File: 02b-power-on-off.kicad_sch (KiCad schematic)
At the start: 13 parts, among them Q1 DMG2305UX-7, Q2 DMG2305UX-7, Q3 BSS138, SW5 SW_Push

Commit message: Add proper charging detection, fix zener footprint
Connect the BQ25 status pin to the microcontroller for a proper
charging detection (low active).
Correct the footprint for the selected zener diode.
Somehow, the wrong footprint got assigned.
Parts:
- D6: footprint Diode_SMD:Nexperia_CFP3_SOD-123W -> prj-footprints:DIO_TDZVT_ROM
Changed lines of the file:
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@@
 			)
 		)
-		(property "Footprint" "Diode_SMD:Nexperia_CFP3_SOD-123W"
+		(property "Footprint" "prj-footprints:DIO_TDZVT_ROM"
 			(at 209.55 120.65 0)
 			(effects

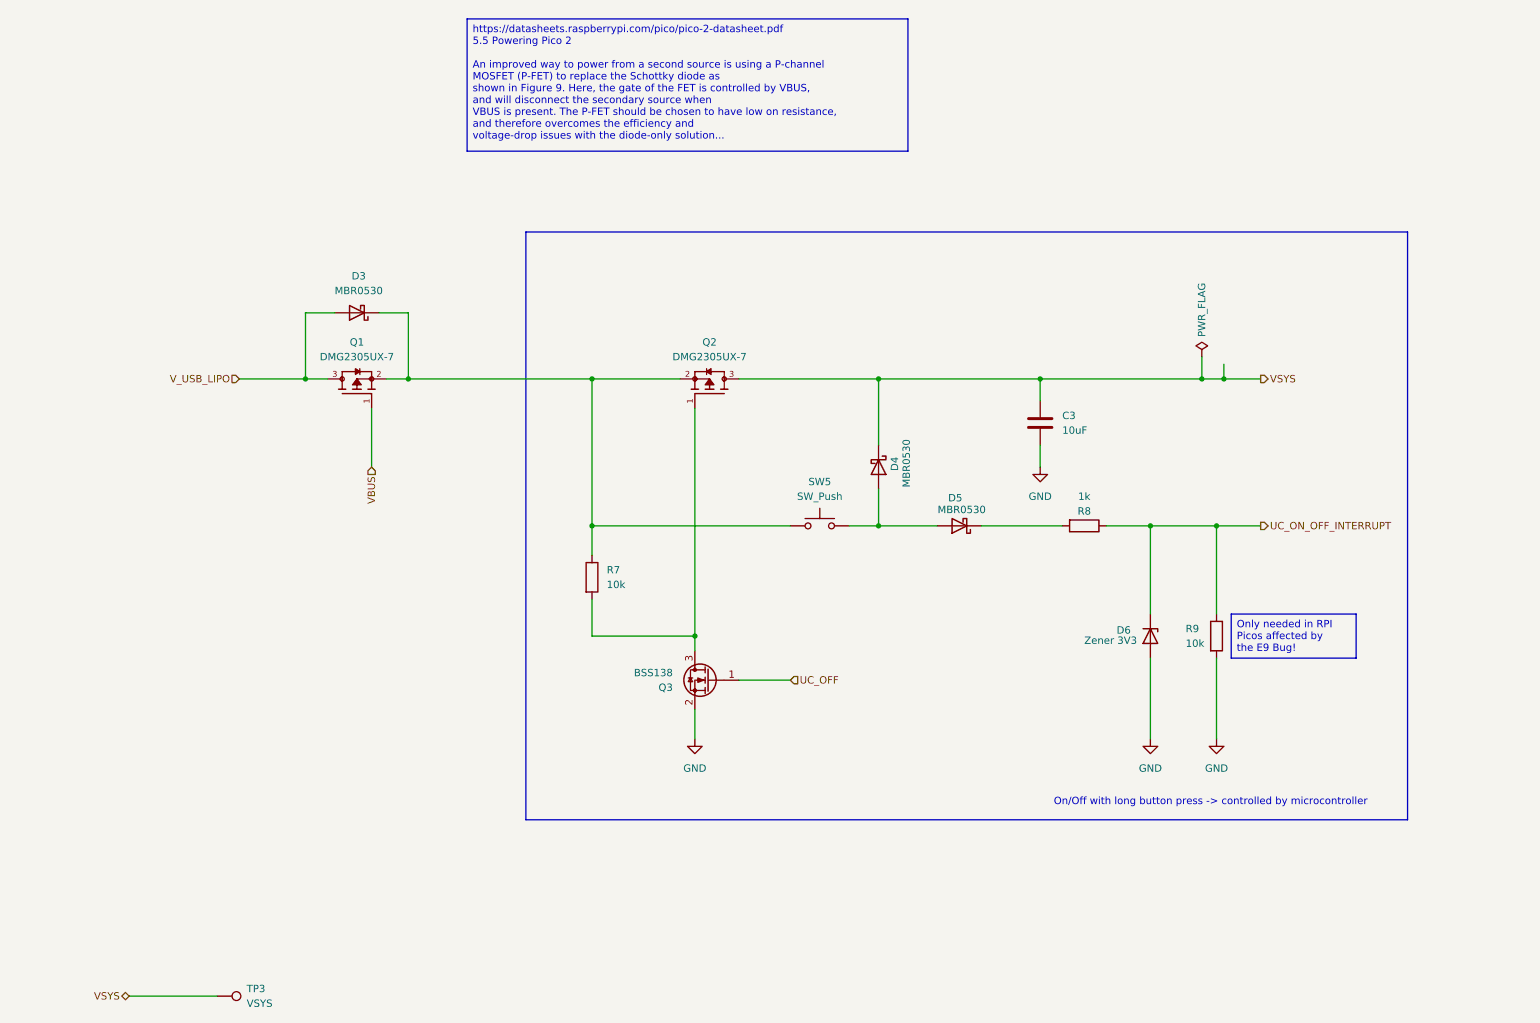
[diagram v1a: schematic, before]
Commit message: Add an voltage bypass mode when USB-C is connected
When USB-C is connected, the device should be charging, but also powered,
without taking care of the on/off button's state.
Otherwise, flashing the device via USB-C would only be
possible as long as the button is pressed which makes the usage
experience a mess and flaky.
This uses p-MOSFETs to do the switch and
a) avoid a battery voltage going to the system when USB-C is connected
b) avoid powering having both, USB-C and Micro-USB active

TODO: This adds the basic idea, routing must be fixed!
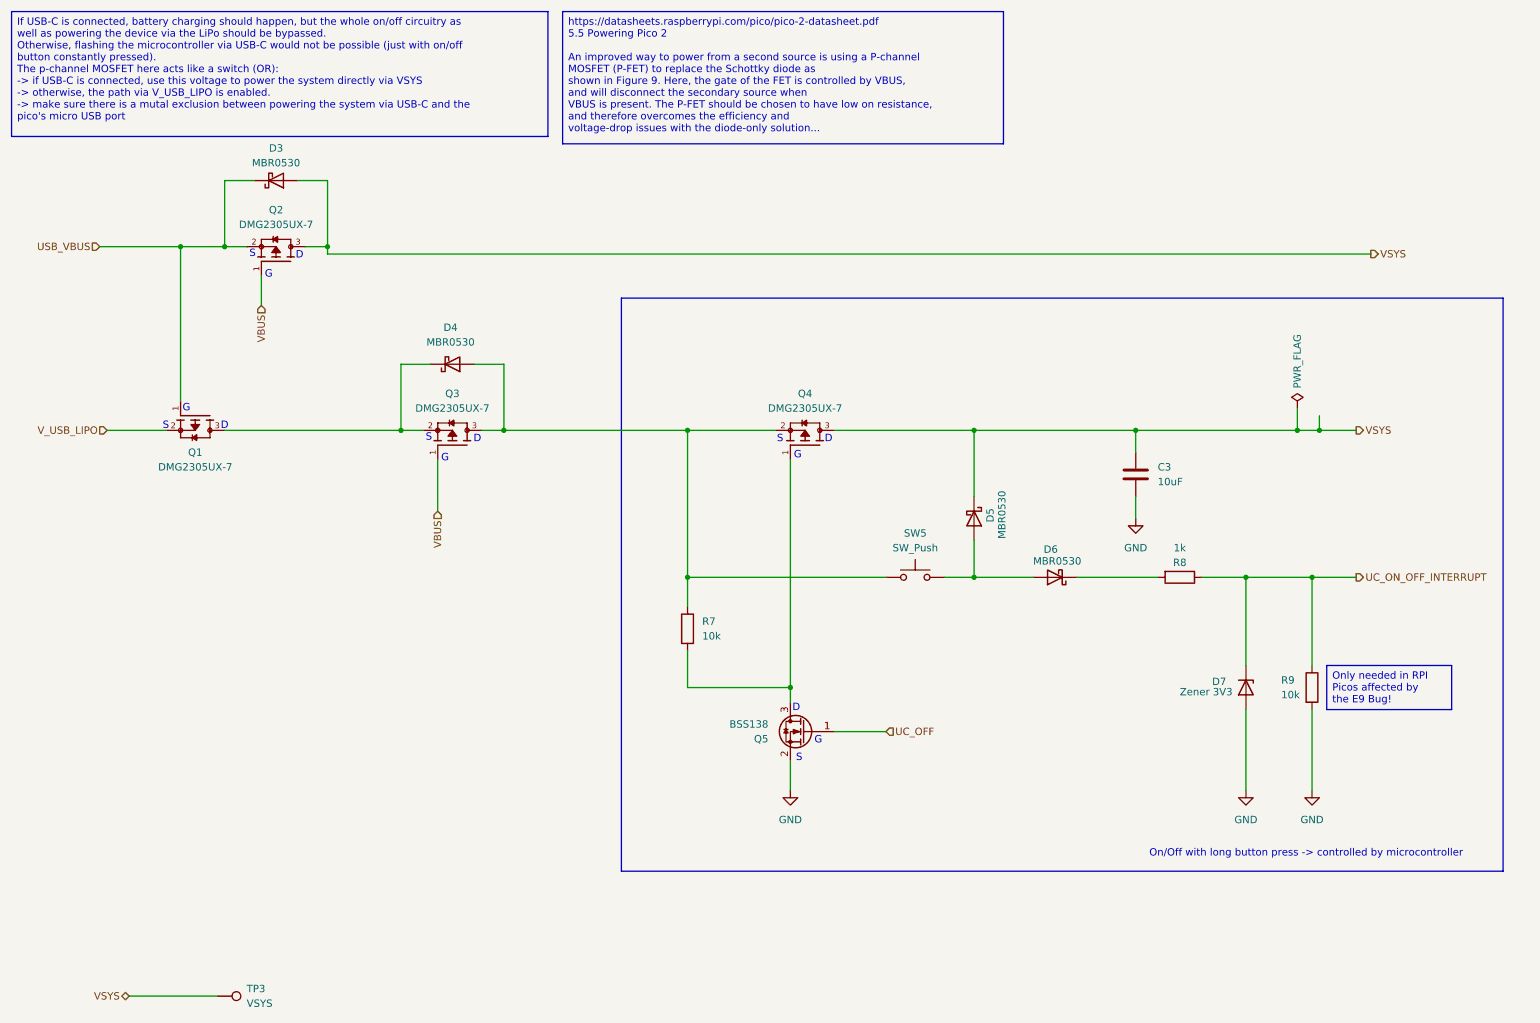
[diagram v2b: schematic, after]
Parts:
- added D3: MBR0530, Diode_SMD:D_SOD-123, symbol Diode:MBR0530
- added Q1, Q2: DMG2305UX-7, Package_TO_SOT_SMD:SOT-23-3, symbol DMG2305UX-7:DMG2305UX-7
- renumbered D3 to D4, D4 to D5, D5 to D6, D6 to D7, Q1 to Q3, Q2 to Q4, Q3 to Q5
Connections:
- net VBUS: now also Q2.1
- net VSYS: now also D3.2 (A), Q2.3
- net V_USB_LIPO: now also Q1.2; no longer D4.2 (A), Q3.3
- net at Q4.2, R7.1, SW5.1: now also D4.2 (A), Q3.3; no longer D4.1 (K), Q3.2
- new net: D4.1 (K), Q1.3, Q3.2
- new net USB_VBUS: D3.1 (K), Q1.1, Q2.2
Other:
- note added: "D"
- note added: "G"
- note added: "S"
- moved on the sheet: C3, D4, D5, D6, D7, Q3, Q4, Q5, R7, R8, R9, SW5

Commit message: Introduce KiCad native Jobsets as an alternative to KiBot
Adds KiCad a jobset together with a new GitHub workflow file
to generate the project outputs without external tooling.

Some general work on the USB-Powerpath routing.
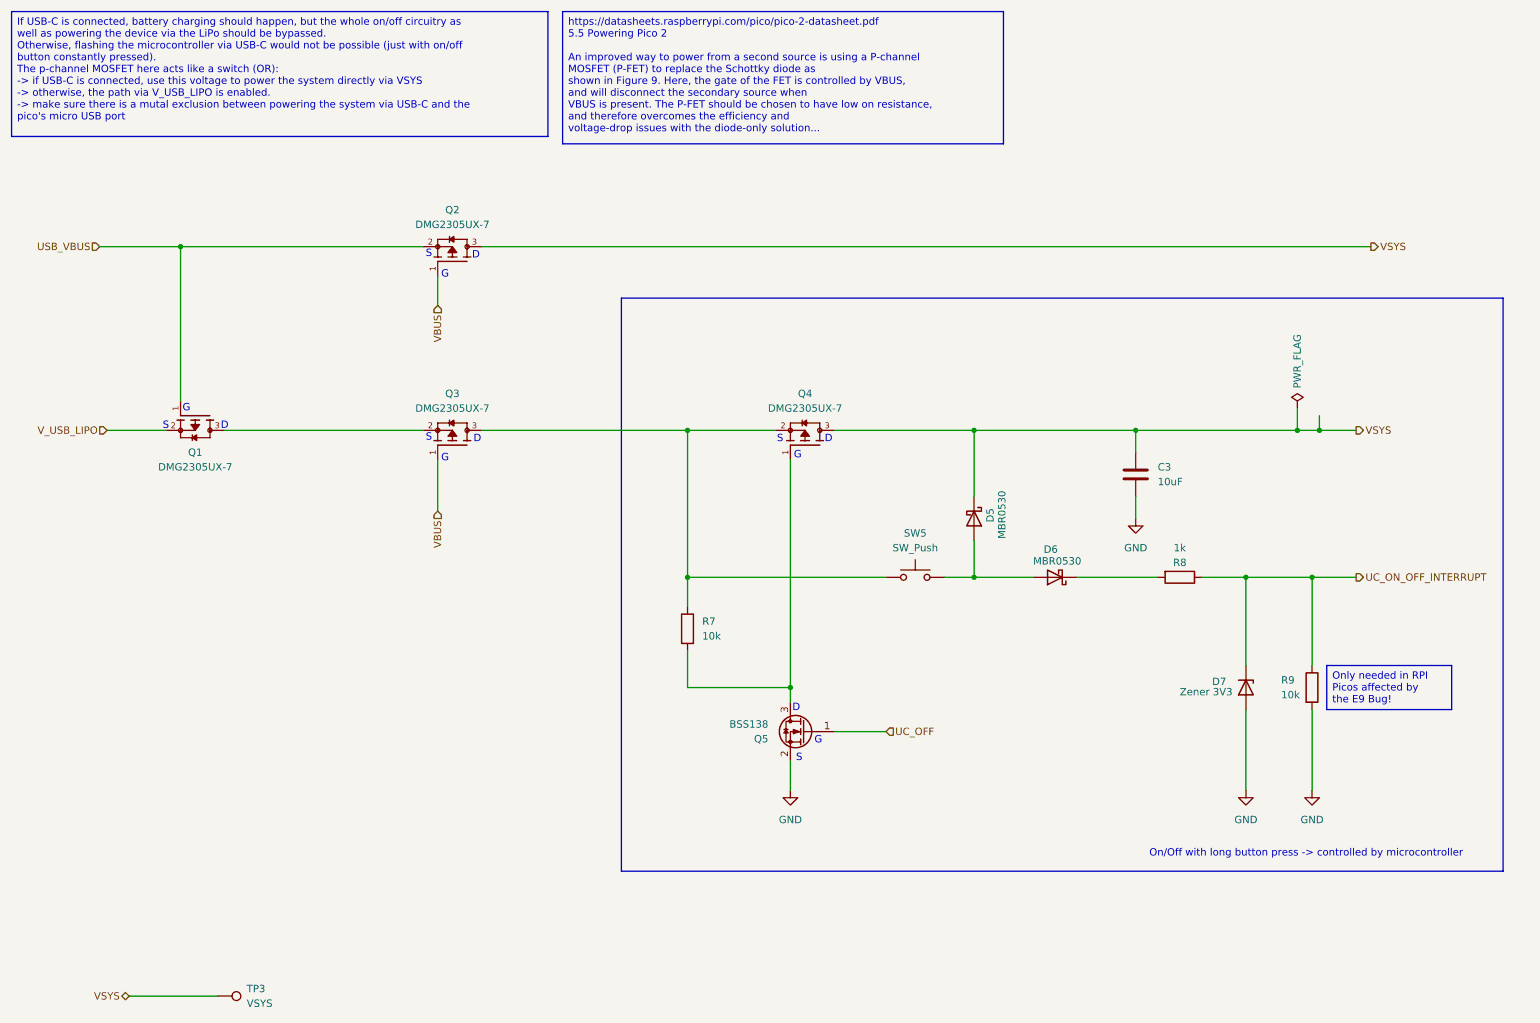
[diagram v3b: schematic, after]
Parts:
- removed D3, D4: MBR0530, Diode_SMD:D_SOD-123, symbol Diode:MBR0530
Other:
- moved on the sheet: Q2
